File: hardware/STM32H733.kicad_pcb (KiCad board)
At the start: 4 copper layers, 38 x 38 mm, 83 parts, among them IC1 AT7456E, J1 USB, J2 DJI, J3 SWD, J5 Conn_01x06_MountingPin, J7 GPS, J8 ESC, J9 ELRS, U1 STM32H733VGTx, U2 ICM-42688-P, U3 TLV75733PDBV, U4 TJA1051TK-3, U5 BMP280, U6 W25Q128JVP, U7 LMR51430, U8 LMR51430, Y1 Resonator_Small, Y2 27MHz

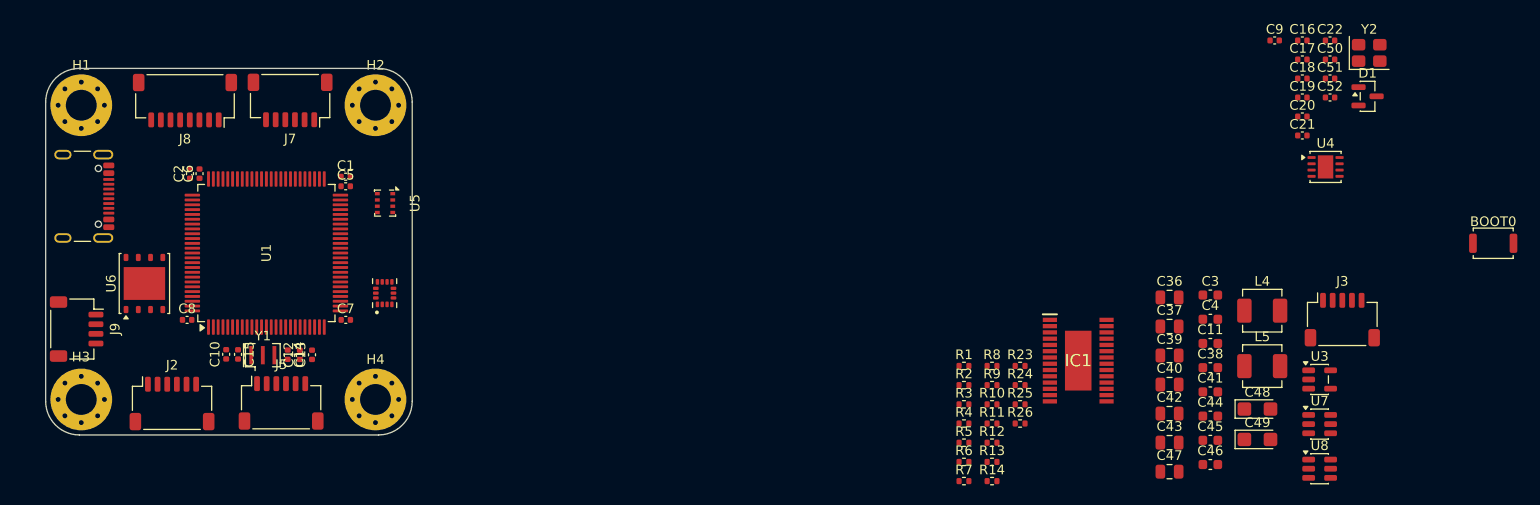
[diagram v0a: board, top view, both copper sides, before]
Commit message: Signed-off-by: Asraful Islam Taj <asraful.islam.taj@gmail.com>
Mostly Done. Need to Fix some Warnings, Need to add Soldering Pad for
CANH and CANL, need to add few pads for UART, I2C, SPI for future use
Need some Test Pads for power
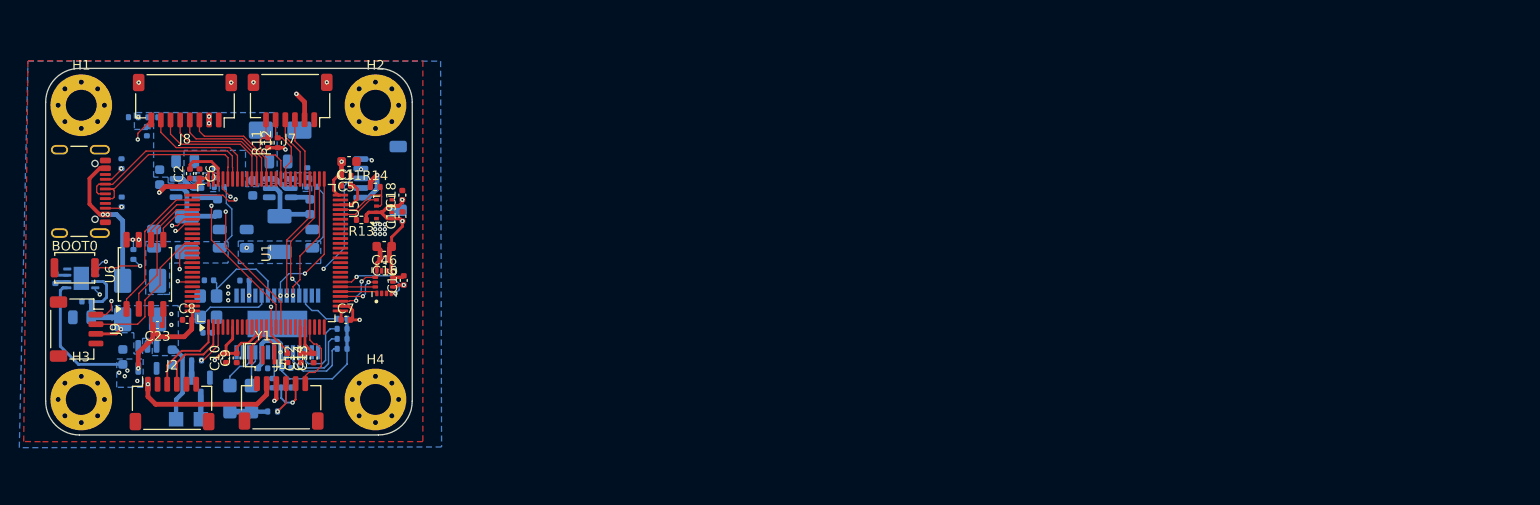
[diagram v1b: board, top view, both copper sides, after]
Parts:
- removed D1: BAT54C, Package_TO_SOT_SMD:SOT-23
- added C23: .1u, Capacitor_SMD:C_0402_1005Metric, F.Cu at (68.9, 114.3)
- added C24: C_Small, Capacitor_SMD:C_0402_1005Metric, B.Cu at (67.8, 94.2)
- added D3: SS34, Diode_SMD:D_SMA, B.Cu at (68.9, 111.7)
- added D4: SMAJ36A, Diode_SMD:D_SMA, B.Cu at (81.6, 94.1)
- added D5: SS34, Diode_SMD:D_SMA, B.Cu at (65.3, 111.7)
- added J4: Conn_01x01_Pin, TestPoint:TestPoint_Pad_1.5x1.5mm, B.Cu at (73.4, 124.0)
- added J6: Conn_01x01_Pin, TestPoint:TestPoint_Pad_1.5x1.5mm, B.Cu at (70.8, 124.1)
- added Q1: SS8050, Package_TO_SOT_SMD:SOT-23, B.Cu at (73.4, 120.7)
- added R15: 1K, Resistor_SMD:R_0402_1005Metric, B.Cu at (73.0, 118.0)
- added R16: 100K, Resistor_SMD:R_0402_1005Metric, B.Cu at (68.4, 92.8)
- added R17: 10K, Resistor_SMD:R_0402_1005Metric, B.Cu at (66.4, 92.7)
- C17, C20, C21, C22, C3, C36, C37, C38, C39, C4, C40, C41, C42, C43, C44, C45, C47, C48, C49, C50, C51, C52, IC1, J3, L4, L5, R1, R10, R2, R23, R24, R25, R26, R3, R4, R5, R6, R7, R8, R9, U3, U4, U7, U8, Y2: moved to B.Cu
- U6: value W25Q128JVP -> W25Q128JVS; footprint Package_SON:WSON-8-1EP_6x5mm_P1.27mm_EP3.4x4.3mm -> Package_SO:SOIC-8_5.3x5.3mm_P1.27mm
- moved BOOT0 147.1 mm to (60.3, 108.3)
- moved U4 129.5 mm to (61.0, 109.5), turned to 180 degrees
- moved C17 128.5 mm to (61.5, 111.8)
- moved Y2 123.2 mm to (74.2, 112.4), turned to 90 degrees
- moved U3 121.5 mm to (67.9, 117.6), turned to -90 degrees
- moved U7 119.9 mm to (72.0, 100.1)
- moved C51 119.3 mm to (74.1, 115.1)
- moved C52 117.7 mm to (74.2, 109.6), turned to 180 degrees
- moved C22 115.2 mm to (77.9, 109.7)
- moved C50 114.7 mm to (80.8, 120.3), turned to -90 degrees
- moved C47 113.9 mm to (61.1, 113.5), turned to 180 degrees
- moved C4 112.8 mm to (65.3, 117.6), turned to -90 degrees
- moved C9 112.5 mm to (77.1, 117.7), turned to 90 degrees
- moved C45 112.3 mm to (69.1, 99.0), turned to 90 degrees
- moved L4 111.8 mm to (72.0, 104.9), turned to -90 degrees
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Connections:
- C17 pad 2: +B5V -> /5V_SYS
- C20 pad 2: +B5V -> /5V_SYS
- C21 pad 2: +B5V -> /5V_SYS
- C22 pad 2: +B5V -> /5V_SYS
- C3 pad 1: Net-(U3-EN) -> /5V_SYS
- C39 pad 1: +B5V -> GND
- C39 pad 2: GND -> +B5V
- C47 pad 1: +B5V -> /5V_SYS
- IC1 pad 10: /OSD_SCK -> /OSD_SCK2
- IC1 pad 11: /OSD_MISO -> /OSD_MISO2
- IC1 pad 21: +B5V -> /5V_SYS
- IC1 pad 24: +B5V -> /5V_SYS
- IC1 pad 3: +B5V -> /5V_SYS
- IC1 pad 8: /OSD_CS -> /OSD_NSS2
- IC1 pad 9: /OSD_MOSI -> /OSD_MOSI2
- J5 pad 3: +B5V -> /5V_SYS
- J7 pad 2: +B5V -> /5V_SYS
- J7 pad 3: /GPS_USART1_RX -> /GPS_USART3_TX
- J7 pad 4: /GPS_USART1_TX -> /GPS_USART3_RX
- J7 pad 5: /GPS_I2C1_SCL -> /GPS_SCL4
- J7 pad 6: /GPS_I2C1_SDA -> /GPS_SDA4
- J8 pad 7: /TLM -> /TLM_RX1
- J8 pad 8: /ACD_CURR -> /ADC_CURR
- J9 pad 3: +B5V -> /5V_SYS
- R10 pad 1: +B5V -> /5V_SYS
- R11 pad 2: /GPS_I2C1_SCL -> /GPS_SDA4
- R12 pad 2: /GPS_I2C1_SDA -> /GPS_SCL4
- R13 pad 2: /BARO_I2C2_SCL -> /BARO_SCL2
- R14 pad 2: /BARO_I2C2_SDA -> /BARO_SDA2
- R7 pad 1: +B5V -> /5V_SYS
- R8 pad 1: +B5V -> /5V_SYS
- R9 pad 1: +B5V -> /5V_SYS
- U1 pad 15: unconnected-(U1-PC0-Pad15) -> /ADC_CURR
- U1 pad 16: unconnected-(U1-PC1-Pad16) -> /VBAT_ADC
- U1 pad 3: unconnected-(U1-PE4-Pad3) -> /BUZZ_GPIO
- U1 pad 46: /SCL2 -> /BARO_SCL2
- U1 pad 47: /SDA2 -> /BARO_SDA2
- U1 pad 51: /NSS2 -> /OSD_NSS2
- U1 pad 52: /SCK2 -> /OSD_SCK2
- U1 pad 53: /MISO2 -> /OSD_MISO2
- U1 pad 54: /MOSI2 -> /OSD_MOSI2
- U1 pad 55: /GPS_USART1_TX -> /GPS_USART3_TX
- U1 pad 56: /GPS_USART1_RX -> /GPS_USART3_RX
- U1 pad 59: unconnected-(U1-PD12-Pad59) -> /GPS_SCL4
- U1 pad 60: unconnected-(U1-PD13-Pad60) -> /GPS_SDA4
- U1 pad 69: /RX1 -> /TLM_RX1
- U3 pad 1: Net-(U3-EN) -> /5V_SYS
- U3 pad 3: Net-(U3-EN) -> /5V_SYS
- U4 pad 3: +B5V -> /5V_SYS
- U5 pad 3: /BARO_I2C2_SDA -> /BARO_SDA2
- U5 pad 4: /BARO_I2C2_SCL -> /BARO_SCL2
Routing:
- net +3.3V: track 0.00 -> 154.5 mm, vias 0 -> 16
- net /5V_SYS: track 0.00 -> 82.1 mm, vias 0 -> 7
- net +B9V: track 0.00 -> 44.1 mm, vias 0 -> 2
- net /ADC_CURR: track 0.00 -> 28.4 mm, vias 0 -> 2
- net /VBAT_ADC: track 0.00 -> 27.9 mm, vias 0 -> 2
- net /NRST: track 0.00 -> 24.6 mm, vias 0 -> 2
- net /SWCLK: track 0.00 -> 22.2 mm, vias 0 -> 2
- net /USB_DN: track 0.00 -> 19.8 mm
- net /USB_DP: track 0.00 -> 19.2 mm
- net /SWDIO: track 0.00 -> 16.9 mm, vias 0 -> 2
- net /FDCAN1_RX: track 0.00 -> 15.7 mm, vias 0 -> 2
- net /RC_USART2_TX: track 0.00 -> 15.5 mm
- net +5VUSB: track 0.00 -> 15.4 mm, vias 0 -> 2
- net /FLASH_NSS3: track 0.00 -> 15.1 mm
- net /OSD_NSS2: track 0.00 -> 14.9 mm, vias 0 -> 2
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- added copper zone on B.Cu, net +3.3V
- added copper zone on In2.Cu, net +3.3V
- added copper zone on B.Cu, net +B5V
- added copper zone on B.Cu, net +B9V
- added copper zone on B.Cu, net /5V_SYS
- added copper zone on In2.Cu, net /5V_SYS
- added copper zone on B.Cu, net /VBAT
- added copper zone on B.Cu, net /VBAT_ADC
- added copper zone on B.Cu, net GND
- added copper zone on F.Cu, net GND
- added copper zone on In1.Cu, net GND
- added copper zone on B.Cu, net Net-(U7-FB)
- added copper zone on B.Cu, net Net-(U8-FB)

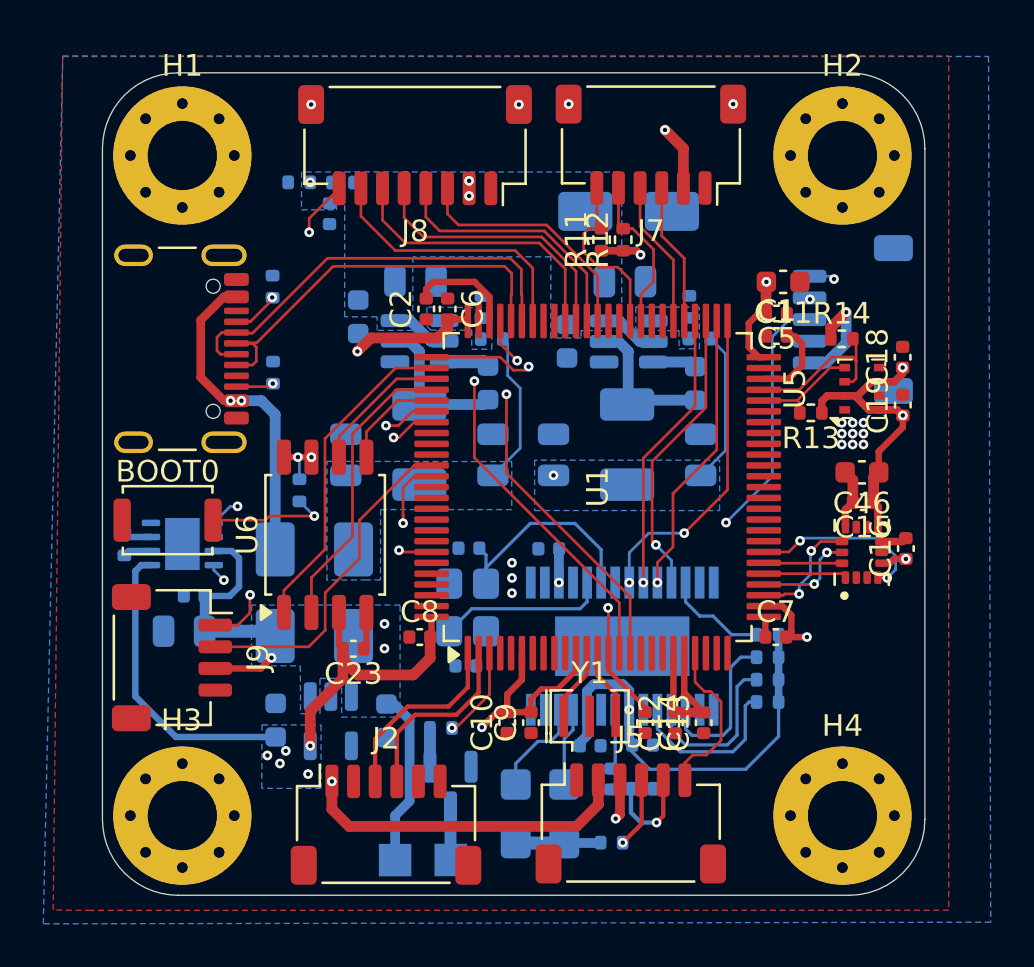
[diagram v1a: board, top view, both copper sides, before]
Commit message: Flight Controller:
Almost Done With the PCB design Except the Leds
and Few Peripherals Pad for external Sensors
and modules

Signed-off-by: Asraful Islam Taj <asraful.islam.taj@gmail.com>
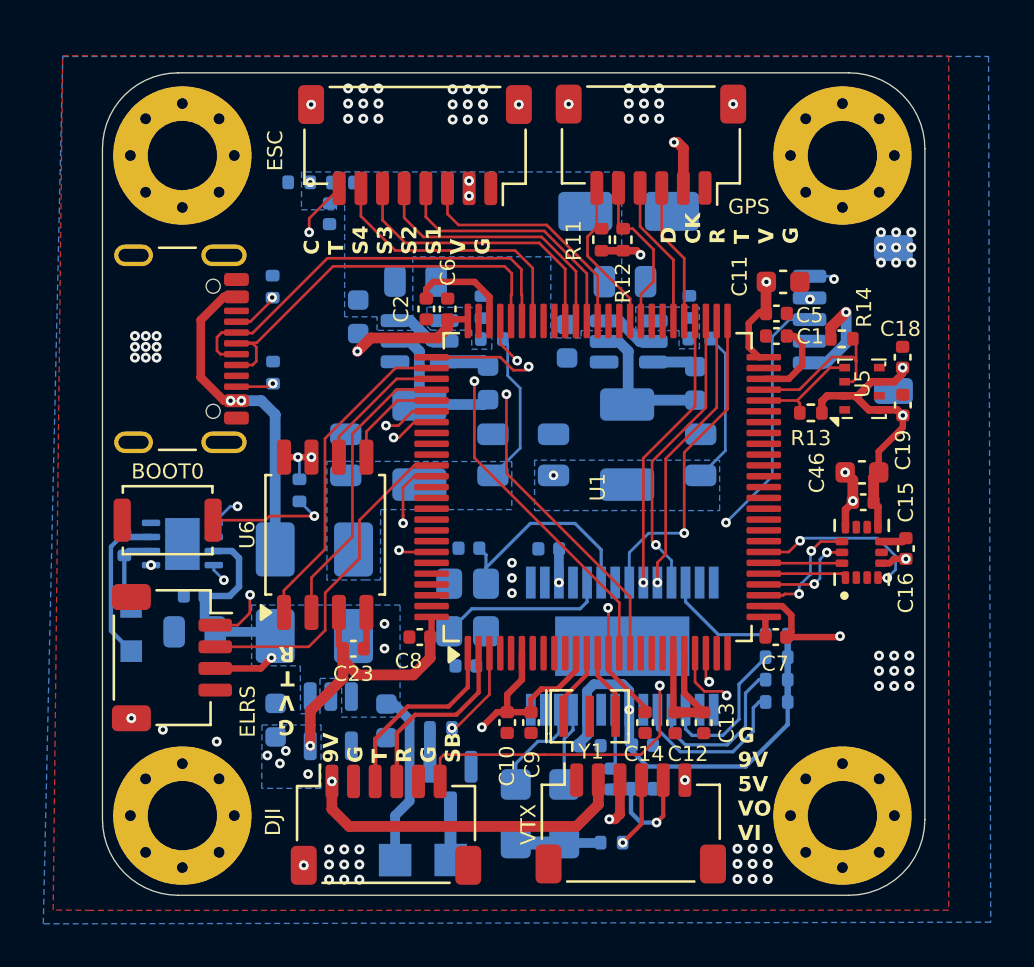
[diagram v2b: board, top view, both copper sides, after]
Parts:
- added J10: CH, TestPoint:TestPoint_Pad_1.0x1.0mm, B.Cu at (58.6, 114.4)
- added J11: CL, TestPoint:TestPoint_Pad_1.0x1.0mm, B.Cu at (58.6, 112.4)
- C24: value C_Small -> 33nF
- J5: value Conn_01x06_MountingPin -> VTX
- moved C47 0.49 mm to (61.6, 113.5)
- moved R10 0.42 mm to (88.5, 113.6)
- moved R7 0.42 mm to (88.5, 116.8)
- moved R8 0.42 mm to (88.5, 115.7)
- moved R9 0.42 mm to (88.5, 114.7)
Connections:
- J2 pad 6: /SBUS -> /SBUS_RX4
- U1 pad 23: /RX4 -> /SBUS_RX4
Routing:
- net /SBUS_RX4: track 0.00 -> 17.7 mm, vias 0 -> 2
- net +3.3V: track 154.5 -> 139.3 mm, vias 16 -> 17
- net /CANH: track 1.30 -> 7.39 mm
- net /CANL: track 1.32 -> 3.83 mm
- net /GPS_SDA4: track 8.33 -> 7.49 mm
- net /TX4: track 7.60 -> 7.76 mm, vias 0 -> 2
- net GND: vias 16 -> 85
- net /OSD_NSS2: vias 2 -> 1
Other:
- board text added: "9V G T R G SB"
- board text added: "C T S4 S3 S2 S1 V G"
- board text added: "D CK R T V G"
- board text added: "G 9V 5V VO VI"
- board text added: "G V T R"

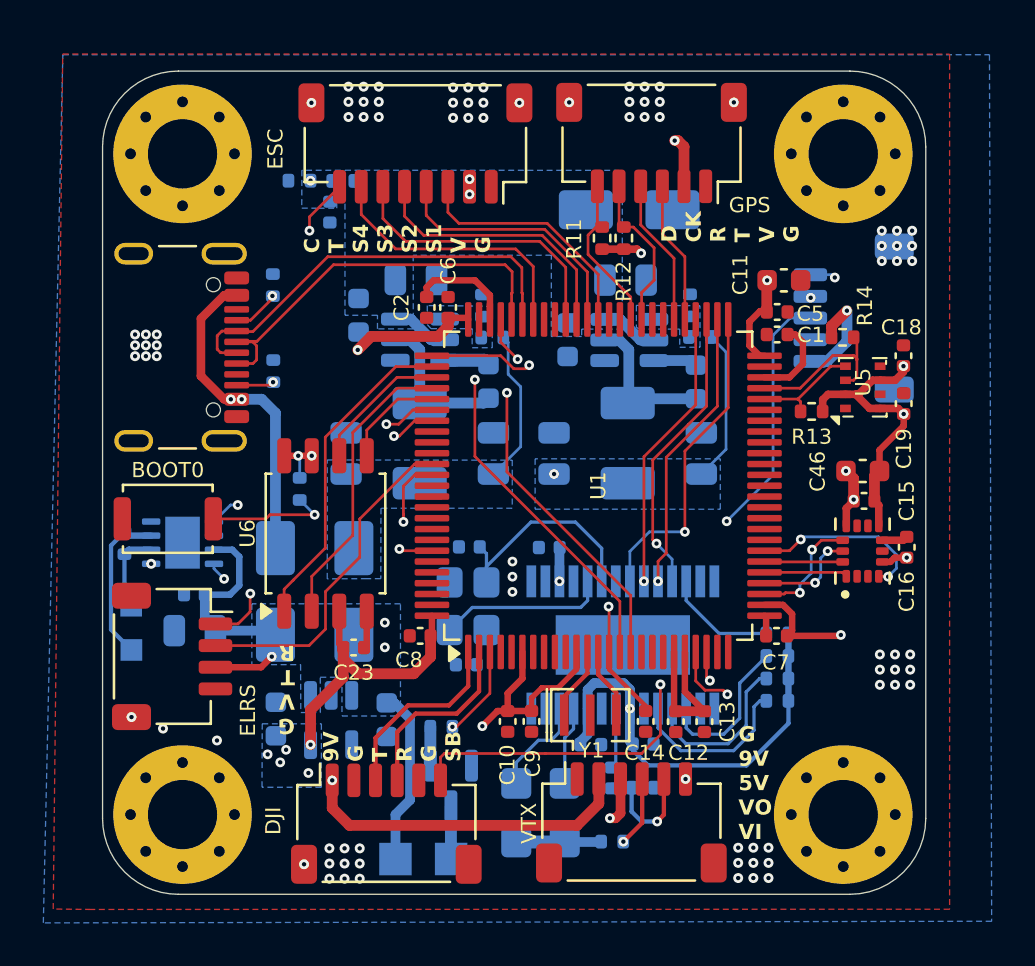
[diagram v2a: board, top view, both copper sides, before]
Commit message: Nebula H7: V 0.1
need to add some indicator led

Signed-off-by: Asraful Islam Taj <asraful.islam.taj@gmail.com>
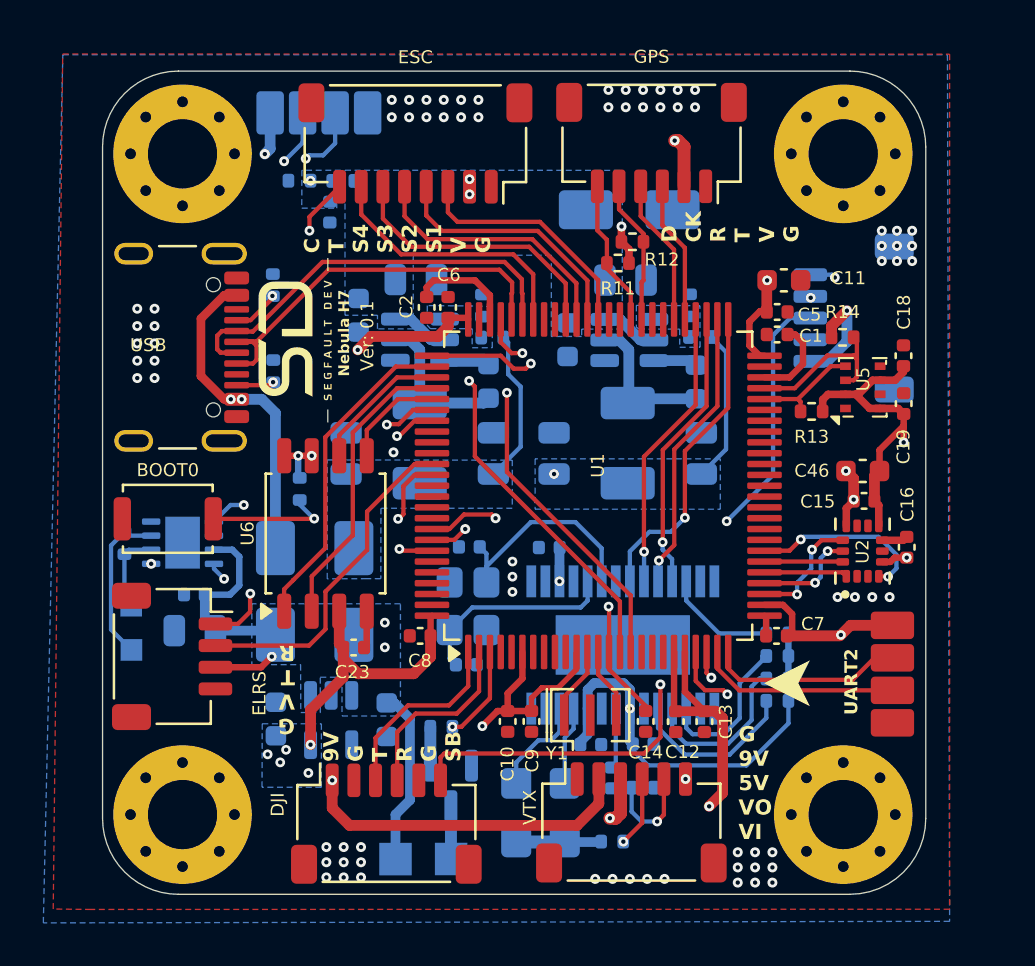
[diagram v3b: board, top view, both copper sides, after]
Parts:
- added G***: LOGO, Custom:logo, F.Cu at (66.7, 100.6)
- added J12: UART2, Custom:ConnPadx04, F.Cu at (101.8, 114.0)
- added J13: I2C1, Custom:ConnPadx04, B.Cu at (65.8, 97.6)
- IC1: footprint user:SOP65P640X120-29N -> User:SOP65P640X120-29N
- U2: footprint user:PQFN50P300X250X97-14N -> User:PQFN50P300X250X97-14N
- moved R11 1.36 mm to (81.1, 96.5), turned to 180 degrees
- moved R12 0.43 mm to (81.8, 95.6), turned to 0 degrees
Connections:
- C12 pad 2: +3.3VA -> +3.3V
- C13 pad 2: +3.3VA -> +3.3V
- U1 pad 20: +3.3VA -> +3.3V
- U1 pad 21: +3.3VA -> +3.3V
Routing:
- net +3.3V: track 139.3 -> 192.9 mm, vias 17 -> 18
- net /SCL1: track 0.00 -> 26.9 mm, vias 0 -> 2
- net /SDA1: track 0.00 -> 24.8 mm, vias 0 -> 2
- net /5V_SYS: track 81.9 -> 98.9 mm
- net /TX2: track 0.00 -> 9.26 mm
- net /RX2: track 0.00 -> 8.98 mm
- net +3.3VA: track 7.20 -> 0.00 mm
- net /GPS_SCL4: track 7.52 -> 6.65 mm
- net /GPS_SDA4: track 7.49 -> 6.78 mm
- net /USB_DN: track 19.8 -> 19.3 mm
- net GND: vias 85 -> 76
- removed copper zone on In2.Cu, net +3.3V
- removed copper zone on In2.Cu, net /5V_SYS
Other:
- board text added: "Nebula H7"
- board text added: "Ver: 0.1"
